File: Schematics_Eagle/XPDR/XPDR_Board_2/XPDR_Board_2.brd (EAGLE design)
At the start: 172.7 x 36.8 mm, 29 parts

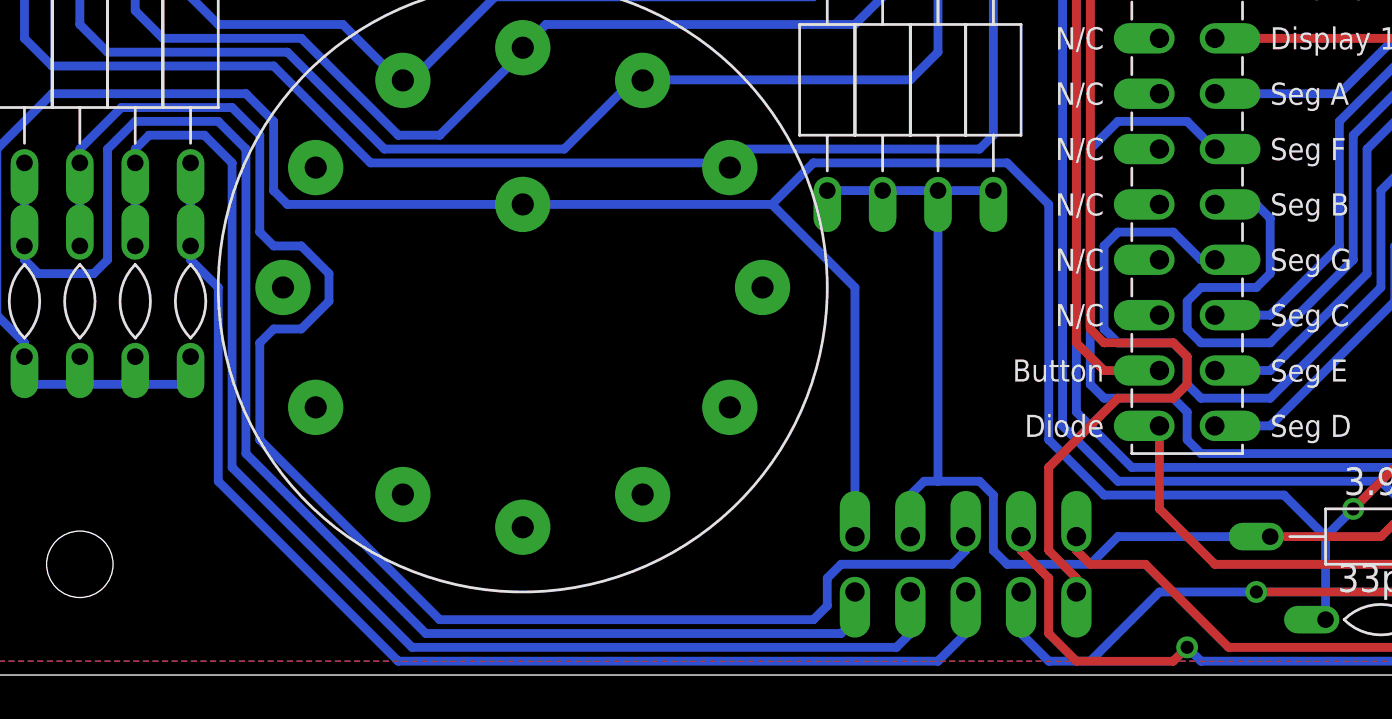
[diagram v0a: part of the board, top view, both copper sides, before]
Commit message: - DME module finished. - Problem with incorrect pins (RST, INT) in XPDR module fixed.
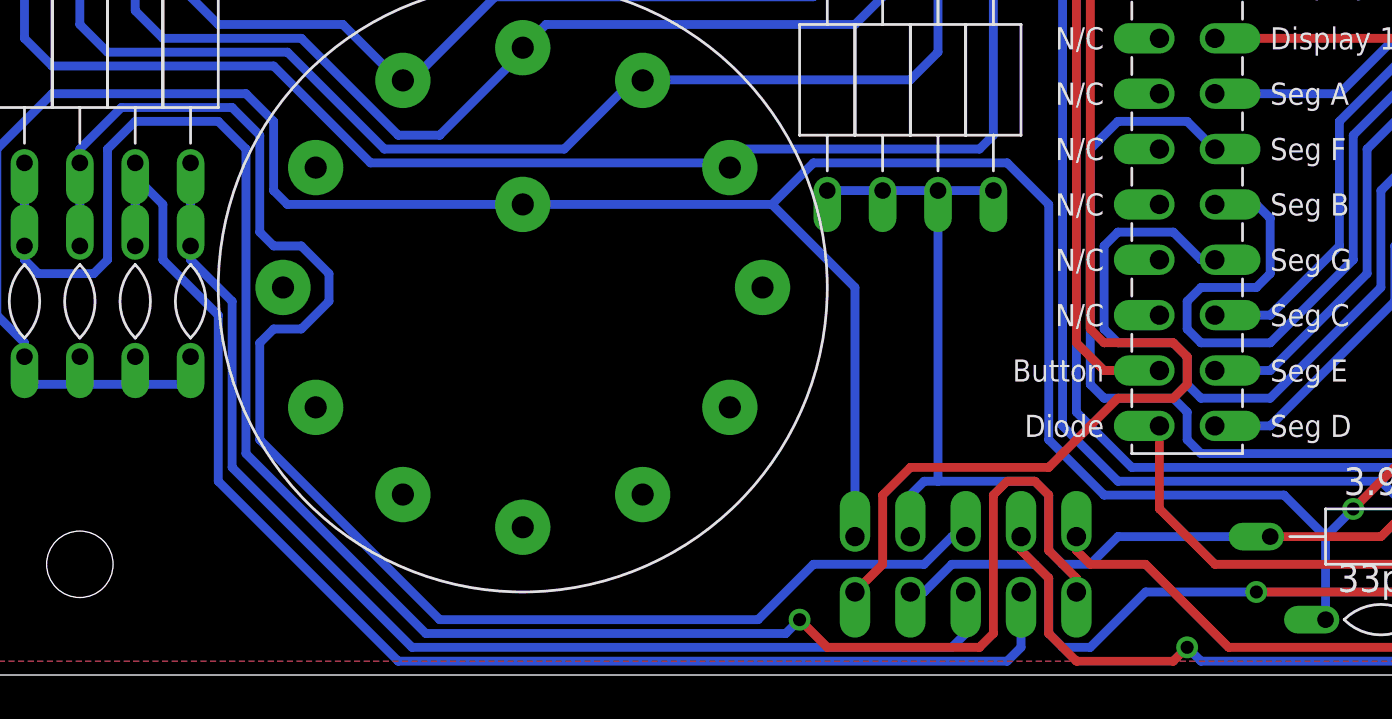
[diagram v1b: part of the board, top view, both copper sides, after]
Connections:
- net N$46: now also U$5.4; no longer U$5.2
- net N$47: now also U$5.5; no longer U$5.1
- net N$55: now also U$5.2; no longer U$5.4
- net N$59: now also U$5.1; no longer U$5.5
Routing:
- net N$59: track 68.1 -> 88.4 mm, vias 0 -> 1
- net N$47: track 111.1 -> 118.0 mm
- net N$46: track 97.1 -> 103.1 mm
- net N$55: track 60.4 -> 62.4 mm
- net N$56: track 55.3 -> 54.0 mm
- net N$54: track 70.6 -> 69.5 mm
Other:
- board text added: "ALT"
- board text added: "ON"
- board text added: "RST"
- board text added: "STBY"
- board text added: "TEST"
- board text removed: "LATCH RST"
- board text removed: "Switch ALT"
- board text removed: "Switch ON"
- board text removed: "Switch STBY"
- board text removed: "Switch TEST"
